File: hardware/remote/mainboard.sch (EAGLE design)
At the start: 11 parts, among them J1 AVR_SPI_PRG_6PTH, U1 ATMEGA328P_VQFNVQFN, U2 RFM69HCW

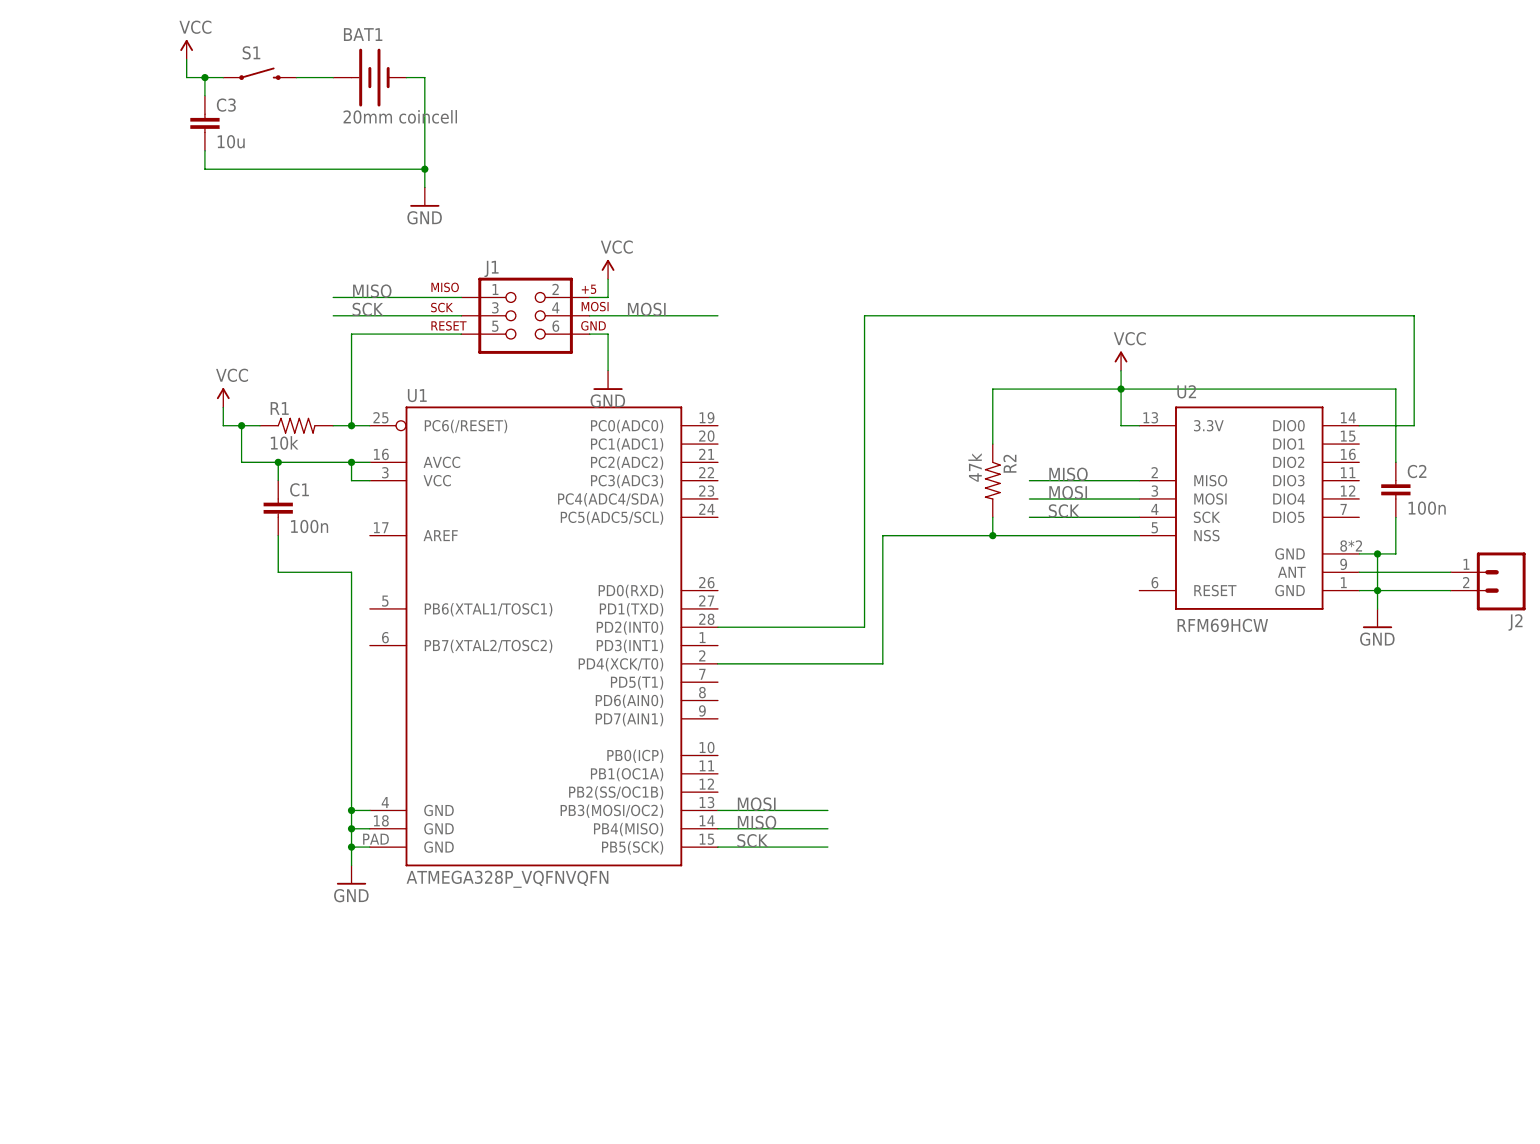
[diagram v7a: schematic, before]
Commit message: Added SPI series impedance and status LED
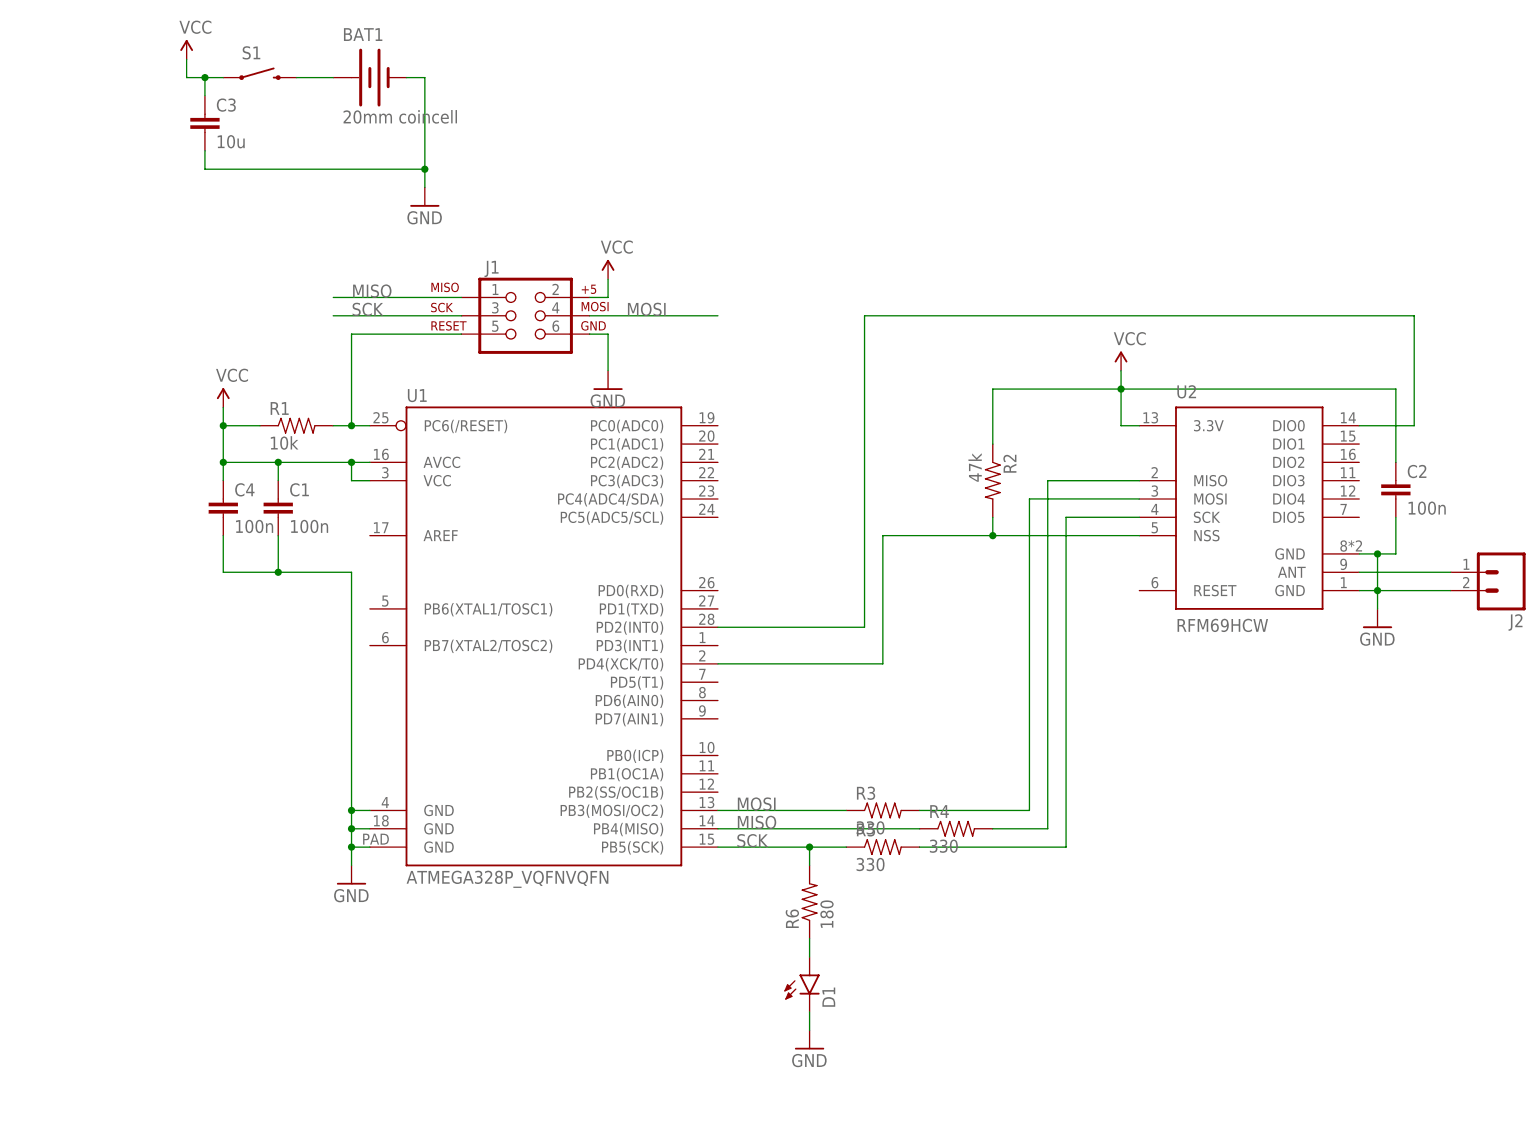
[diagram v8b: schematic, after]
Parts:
- added C4: 100n, SparkFun-Passives:CAP0603-CAP
- added D1: (no value), SparkFun-LED:LED0603
- added R3, R4, R5: 330, SparkFun-Passives:RESISTOR0603-RES
- added R6: 180, SparkFun-Passives:RESISTOR0603-RES
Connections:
- new net N$3: R3.2, U2.MOSI
- new net N$5: R4.2, U2.MISO
- new net N$7: R5.2, U2.SCK
- new net N$9: D1.A, R6.1
- net GND: now also C4.2, D1.C
- net MISO: now also R4.1; no longer U2.MISO
- net MOSI: now also R3.1; no longer U2.MOSI
- net SCK: now also R5.1, R6.2; no longer U2.SCK
- net VCC: now also C4.1
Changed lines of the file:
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@@
 <classes>
 <class number="0" name="default" width="0" drill="0">
+<clearance class="0" value="0.205"/>
 </class>
 </classes>
@@
 <part name="J2" library="SparkFun-Connectors" deviceset="M02" device="PTH"/>
 <part name="FRAME1" library="frames" deviceset="LETTER_L" device=""/>
+<part name="R3" library="SparkFun-Passives" deviceset="RESISTOR" device="0603-RES" value="330"/>
+<part name="R4" library="SparkFun-Passives" deviceset="RESISTOR" device="0603-RES" value="330"/>
+<part name="R5" library="SparkFun-Passives" deviceset="RESISTOR" device="0603-RES" value="330"/>
+<part name="R6" library="SparkFun-Passives" deviceset="RESISTOR" device="0603-RES" value="180"/>
+<part name="D1" library="SparkFun-LED" deviceset="LED" device="0603"/>
+<part name="GND5" library="SparkFun-Aesthetics" deviceset="GND" device=""/>
+<part name="C4" library="SparkFun-Passives" deviceset="CAP" device="0603-CAP" value="100n"/>
 </parts>
 <sheets>
@@
 <instance part="FRAME1" gate="G$1" x="0" y="0"/>
 <instance part="FRAME1" gate="G$2" x="147.32" y="0"/>
+<instance part="R3" gate="G$1" x="124.46" y="53.34"/>
+<instance part="R4" gate="G$1" x="134.62" y="50.8"/>
+<instance part="R5" gate="G$1" x="124.46" y="48.26"/>
+<instance part="R6" gate="G$1" x="114.3" y="40.64" rot="R90"/>
+<instance part="D1" gate="G$1" x="114.3" y="30.48"/>
+<instance part="GND5" gate="1" x="114.3" y="20.32"/>
+<instance part="C4" gate="G$1" x="33.02" y="93.98"/>
 </instances>
 <busses>
@@
 <wire x1="33.02" y1="109.22" x2="33.02" y2="106.68" width="0.1524" layer="91"/>
 <pinref part="R1" gate="G$1" pin="1"/>
-<wire x1="33.02" y1="106.68" x2="35.56" y2="106.68" width="0.1524" layer="91"/>
 <pinref part="U1" gate="G$1" pin="VCC"/>
-<wire x1="35.56" y1="106.68" x2="38.1" y2="106.68" width="0.1524" layer="91"/>
+<wire x1="33.02" y1="106.68" x2="38.1" y2="106.68" width="0.1524" layer="91"/>
 <wire x1="53.34" y1="99.06" x2="50.8" y2="99.06" width="0.1524" layer="91"/>
 <wire x1="50.8" y1="99.06" x2="50.8" y2="101.6" width="0.1524" layer="91"/>
 <wire x1="50.8" y1="101.6" x2="40.64" y2="101.6" width="0.1524" layer="91"/>
-<wire x1="40.64" y1="101.6" x2="35.56" y2="101.6" width="0.1524" layer="91"/>
-<wire x1="35.56" y1="101.6" x2="35.56" y2="106.68" width="0.1524" layer="91"/>
-<junction x="35.56" y="106.68"/>
+<wire x1="40.64" y1="101.6" x2="33.02" y2="101.6" width="0.1524" layer="91"/>
+<wire x1="33.02" y1="101.6" x2="33.02" y2="106.68" width="0.1524" layer="91"/>
+<junction x="33.02" y="106.68"/>
 <pinref part="U1" gate="G$1" pin="AVCC"/>
 <wire x1="53.34" y1="101.6" x2="50.8" y2="101.6" width="0.1524" layer="91"/>
@@
 <wire x1="40.64" y1="99.06" x2="40.64" y2="101.6" width="0.1524" layer="91"/>
 <junction x="40.64" y="101.6"/>
+<pinref part="C4" gate="G$1" pin="1"/>
+<wire x1="33.02" y1="99.06" x2="33.02" y2="101.6" width="0.1524" layer="91"/>
+<junction x="33.02" y="101.6"/>
 </segment>
 <segment>
@@
 <wire x1="50.8" y1="86.36" x2="50.8" y2="53.34" width="0.1524" layer="91"/>
 <junction x="50.8" y="53.34"/>
+<pinref part="C4" gate="G$1" pin="2"/>
+<wire x1="33.02" y1="91.44" x2="33.02" y2="86.36" width="0.1524" layer="91"/>
+<wire x1="33.02" y1="86.36" x2="40.64" y2="86.36" width="0.1524" layer="91"/>
+<junction x="40.64" y="86.36"/>
 </segment>
 <segment>
@@
 <junction x="193.04" y="88.9"/>
 </segment>
+<segment>
+<pinref part="D1" gate="G$1" pin="C"/>
+<pinref part="GND5" gate="1" pin="GND"/>
+<wire x1="114.3" y1="25.4" x2="114.3" y2="22.86" width="0.1524" layer="91"/>
+</segment>
 </net>
 <net name="N$2" class="0">
@@
 <segment>
 <pinref part="U1" gate="G$1" pin="PB5(SCK)"/>
-<wire x1="101.6" y1="48.26" x2="116.84" y2="48.26" width="0.1524" layer="91"/>
+<wire x1="101.6" y1="48.26" x2="114.3" y2="48.26" width="0.1524" layer="91"/>
 <label x="104.14" y="48.26" size="1.778" layer="95"/>
-</segment>
-<segment>
-<pinref part="U2" gate="G$1" pin="SCK"/>
-<wire x1="160.02" y1="93.98" x2="144.78" y2="93.98" width="0.1524" layer="91"/>
-<label x="147.32" y="93.98" size="1.778" layer="95"/>
+<pinref part="R5" gate="G$1" pin="1"/>
+<pinref part="R6" gate="G$1" pin="2"/>
+<wire x1="114.3" y1="48.26" x2="119.38" y2="48.26" width="0.1524" layer="91"/>
+<wire x1="114.3" y1="45.72" x2="114.3" y2="48.26" width="0.1524" layer="91"/>
+<junction x="114.3" y="48.26"/>
 </segment>
 <segment>
@@
 <segment>
 <pinref part="U1" gate="G$1" pin="PB4(MISO)"/>
-<wire x1="101.6" y1="50.8" x2="116.84" y2="50.8" width="0.1524" layer="91"/>
+<wire x1="101.6" y1="50.8" x2="129.54" y2="50.8" width="0.1524" layer="91"/>
 <label x="104.14" y="50.8" size="1.778" layer="95"/>
+<pinref part="R4" gate="G$1" pin="1"/>
 </segment>
 <segment>
@@
 <label x="50.8" y="124.46" size="1.778" layer="95"/>
 </segment>
-<segment>
-<pinref part="U2" gate="G$1" pin="MISO"/>
-<wire x1="160.02" y1="99.06" x2="144.78" y2="99.06" width="0.1524" layer="91"/>
-<label x="147.32" y="99.06" size="1.778" layer="95"/>
-</segment>
 </net>
 <net name="MOSI" class="0">
 <segment>
 <pinref part="U1" gate="G$1" pin="PB3(MOSI/OC2)"/>
-<wire x1="101.6" y1="53.34" x2="116.84" y2="53.34" width="0.1524" layer="91"/>
+<wire x1="101.6" y1="53.34" x2="119.38" y2="53.34" width="0.1524" layer="91"/>
 <label x="104.14" y="53.34" size="1.778" layer="95"/>
+<pinref part="R3" gate="G$1" pin="1"/>
 </segment>
 <segment>
@@
 <wire x1="83.82" y1="121.92" x2="101.6" y2="121.92" width="0.1524" layer="91"/>
 <label x="88.9" y="121.92" size="1.778" layer="95"/>
-</segment>
-<segment>
-<pinref part="U2" gate="G$1" pin="MOSI"/>
-<wire x1="160.02" y1="96.52" x2="144.78" y2="96.52" width="0.1524" layer="91"/>
-<label x="147.32" y="96.52" size="1.778" layer="95"/>
 </segment>
 </net>
@@
 </segment>
 </net>
+<net name="N$3" class="0">
+<segment>
+<pinref part="R3" gate="G$1" pin="2"/>
+<wire x1="129.54" y1="53.34" x2="144.78" y2="53.34" width="0.1524" layer="91"/>
+<wire x1="144.78" y1="53.34" x2="144.78" y2="96.52" width="0.1524" layer="91"/>
+<pinref part="U2" gate="G$1" pin="MOSI"/>
+<wire x1="144.78" y1="96.52" x2="160.02" y2="96.52" width="0.1524" layer="91"/>
+</segment>
+</net>
+<net name="N$5" class="0">
+<segment>
+<pinref part="R4" gate="G$1" pin="2"/>
+<wire x1="139.7" y1="50.8" x2="147.32" y2="50.8" width="0.1524" layer="91"/>
+<wire x1="147.32" y1="50.8" x2="147.32" y2="99.06" width="0.1524" layer="91"/>
+<pinref part="U2" gate="G$1" pin="MISO"/>
+<wire x1="147.32" y1="99.06" x2="160.02" y2="99.06" width="0.1524" layer="91"/>
+</segment>
+</net>
+<net name="N$7" class="0">
+<segment>
+<pinref part="R5" gate="G$1" pin="2"/>
+<wire x1="129.54" y1="48.26" x2="149.86" y2="48.26" width="0.1524" layer="91"/>
+<wire x1="149.86" y1="48.26" x2="149.86" y2="93.98" width="0.1524" layer="91"/>
+<pinref part="U2" gate="G$1" pin="SCK"/>
+<wire x1="149.86" y1="93.98" x2="160.02" y2="93.98" width="0.1524" layer="91"/>
+</segment>
+</net>
+<net name="N$9" class="0">
+<segment>
+<pinref part="R6" gate="G$1" pin="1"/>
+<pinref part="D1" gate="G$1" pin="A"/>
+<wire x1="114.3" y1="35.56" x2="114.3" y2="33.02" width="0.1524" layer="91"/>
+</segment>
+</net>
 </nets>
 </sheet>
 </sheets>
-<errors>
-</errors>
 </schematic>
 </drawing>
